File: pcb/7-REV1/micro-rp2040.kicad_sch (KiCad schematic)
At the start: 60 parts, among them J201 Conn_01x03, J202 TYPE-C-31-M-12, Q1 2N7002T, Q5 2N7002T, SW101 TS3425BA 098 2.5H 250gf, SW102 TS3315A 250gf 025, U1 RP2350B, U102 W25Q128JVSIQ, U105 MT29F1G01ABAFDWB, U16 SP3002-04JTG, U3 TLV74311PDBVR, U401 ME6211A33PG-N, U8 APS6404L-3SQR-ZR, Y101 ABM8-272-T3

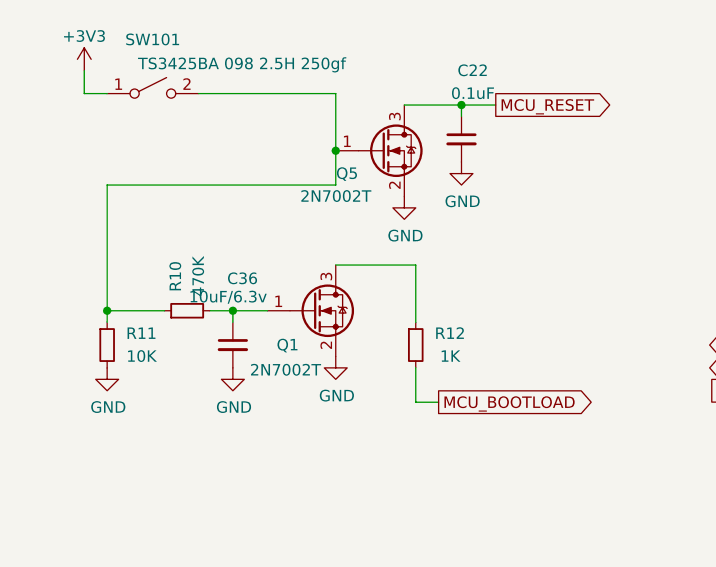
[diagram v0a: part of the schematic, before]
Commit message: specify part numbers and manufacturers in more detail - 10µF / 0805 caps - 2N7002KT fets
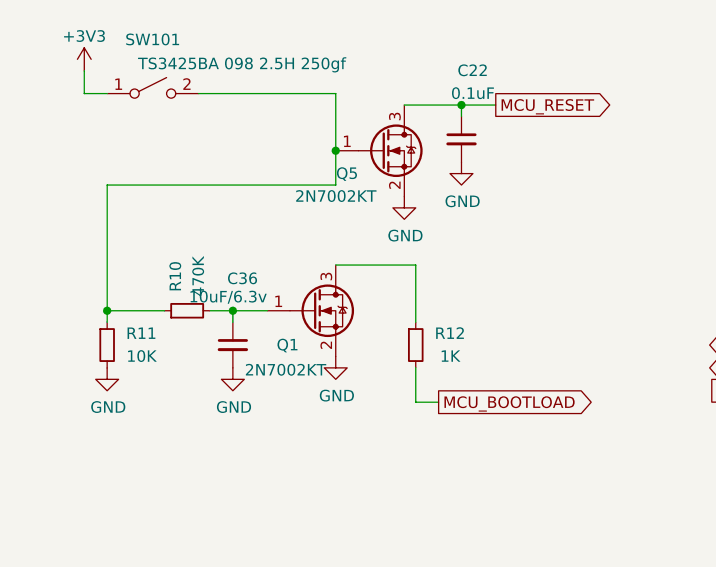
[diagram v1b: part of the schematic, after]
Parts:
- C10, C104, C109, C11, C19, C201, C202, C24, C36, C4, C401, C402: MANUFACTURER (none) -> Samsung
- Q1, Q5: value 2N7002T -> 2N7002KT; MANUFACTURER (none) -> CBI

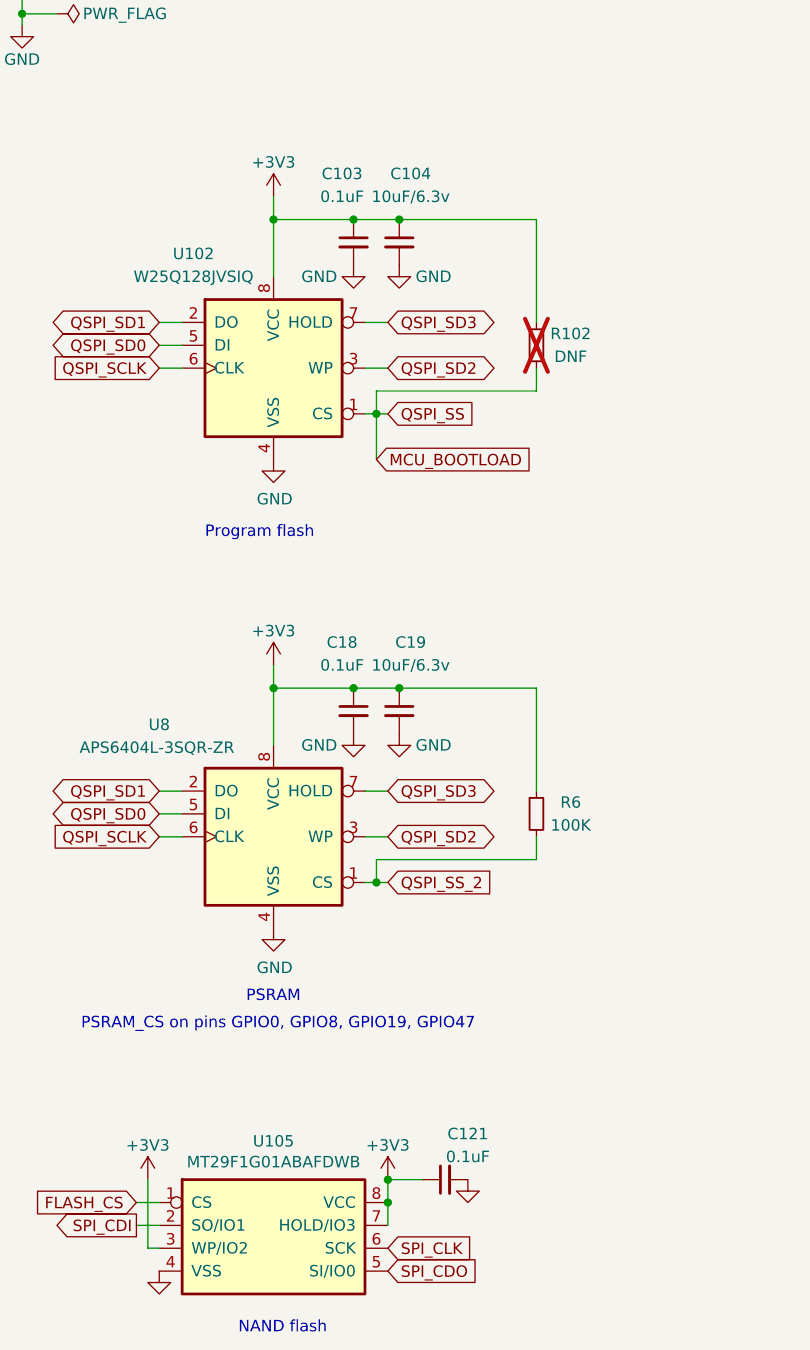
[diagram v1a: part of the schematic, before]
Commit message: improve decoupling for the memory ICs (NOR, NAND, PSRAM) - do not use 100nF 0402 || 10µF 0402 - just use 10µF 0402 - the lowest impedance and resonance freq is mostly determined by size - so the 100nF 0402 will not lower the total impedance - but when the 100nF 0402 is directly next to the Vcc/GND pins,   the 10µF 0402 must be more far away and thus have more inductance
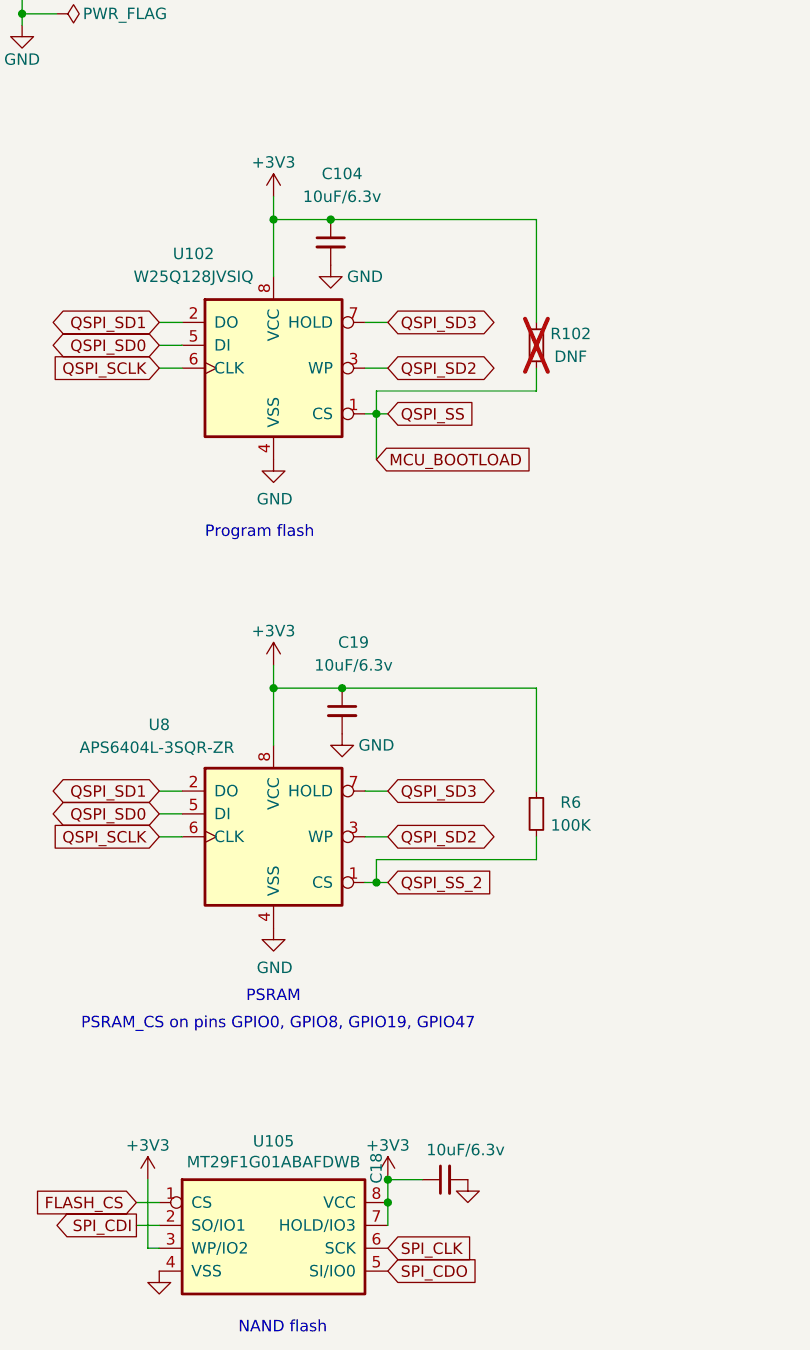
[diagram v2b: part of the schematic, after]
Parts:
- removed C103, C121: 0.1uF, Capacitor_SMD:C_0402_1005Metric, symbol Device:C_Small
- C18: value 0.1uF -> 10uF/6.3v; MANUFACTURER (none) -> Samsung; RMB 0.00628 -> 0.043101; Supplier https://item.szlcsc.com/1877.html -> https://item.szlcsc.com/108589.html
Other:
- moved on the sheet: C104, C19
